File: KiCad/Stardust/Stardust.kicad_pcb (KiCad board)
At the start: 2 copper layers, 7 parts, among them IC1 TS1117BCW50_RPG, U1 ESP32-DEVKITC, U2 TMC2209_SILENTSTEPSTICK, U3 TMC2209_SILENTSTEPSTICK, U4 WEMOS_D1_mini, U5 RTC 3013, U6 MC7812BDTRKG

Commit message: More work on sch and board layout
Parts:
- added J1: Jack-DC, Stardust:DC_PowerConn_694108402002, F.Cu at (189.8, 55.9)
- added J2: 85513-5002, Stardust:RJ12_855135114, F.Cu at (165.0, 58.5)
- added U7: 56200001009, Stardust:FuseHolder_RHDR2W53P0X508_1X2, F.Cu at (183.9, 55.5)
- U1, U2, U3, U4, U5: moved to B.Cu
- moved U4 69.7 mm to (148.4, 59.6), turned to 180 degrees
- moved U2 58.1 mm to (190.5, 115.0)
- moved U5 47.5 mm to (133.3, 114.1), turned to -90 degrees
- moved U1 32.7 mm to (164.3, 100.3), turned to 180 degrees
- moved U3 31.5 mm to (190.7, 93.2)
- moved IC1 25.1 mm to (194.3, 76.0)
- moved U6 14.5 mm to (195.1, 68.5), turned to -90 degrees
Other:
- board outline added: 77 x 77 mm

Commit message: Finished schematic (V1.0)
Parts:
- removed IC1: TS1117BCW50_RPG, Stardust:5VREG_SOT230P700X180-4N
- removed U5: RTC 3013, Stardust:MODULE_3013
- removed U6: MC7812BDTRKG, Stardust:12VREG_DPAK-3_ONS
- added J3: 1x2 Connector, Connector_PinHeader_2.54mm:PinHeader_1x02_P2.54mm_Vertical, F.Cu at (181.0, 73.0)
- added J7: 1x2 Connector, Connector_PinHeader_2.54mm:PinHeader_1x02_P2.54mm_Vertical, F.Cu at (111.6, 53.4)
- added R1: 4.7K, Resistor_SMD:R_0402_1005Metric, F.Cu at (188.0, 79.5)
- added R10: 4.7K, Resistor_SMD:R_0402_1005Metric, F.Cu at (104.9, 58.0)
- added R11: 2.4K, Resistor_SMD:R_0402_1005Metric, F.Cu at (104.9, 60.0)
- added R12: 2.4K, Resistor_SMD:R_0402_1005Metric, F.Cu at (107.8, 52.0)
- added R13: 2.4K, Resistor_SMD:R_0402_1005Metric, F.Cu at (107.8, 54.0)
- added R14: 2.4K, Resistor_SMD:R_0402_1005Metric, F.Cu at (107.8, 56.0)
- added R15: 2.4K, Resistor_SMD:R_0402_1005Metric, F.Cu at (107.8, 58.0)
- added R2: 1K, Resistor_SMD:R_0402_1005Metric, F.Cu at (102.0, 52.0)
- added R3: 4.7K, Resistor_SMD:R_0402_1005Metric, F.Cu at (102.0, 54.0)
- added R4: 4.7K, Resistor_SMD:R_0402_1005Metric, F.Cu at (102.0, 56.0)
- added R5: 4.7K, Resistor_SMD:R_0402_1005Metric, F.Cu at (102.0, 58.0)
- added R6: 4.7K, Resistor_SMD:R_0402_1005Metric, F.Cu at (102.0, 60.0)
- added R7: 4.7K, Resistor_SMD:R_0402_1005Metric, F.Cu at (104.9, 52.0)
- added R8: 4.7K, Resistor_SMD:R_0402_1005Metric, F.Cu at (104.9, 54.0)
- added R9: 4.7K, Resistor_SMD:R_0402_1005Metric, F.Cu at (104.9, 56.0)
- added U8: LittlFuse 2.5 Amp, Stardust:FuseHolder_RHDR2W53P0X508_1X2, F.Cu at (184.5, 68.5)
- J1: value Jack-DC -> 12V DC
- J2: value 85513-5002 -> RJ12
- U1: value ESP32-DEVKITC -> ESP32
- U2, U3: value TMC2209_SILENTSTEPSTICK -> BTT TMC2209 V1.3
- U7: value 56200001009 -> Regulator - 5V 1A; footprint Stardust:FuseHolder_RHDR2W53P0X508_1X2 -> Stardust:5VREG_SOT230P700X180-4N
- moved U7 4.18 mm to (181.5, 58.9)
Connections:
- J1 pad 1: unconnected-(J1-Pad1) -> Net-(J1-Pad1)
- J1 pad 2: unconnected-(J1-Pad2) -> GND
- J1 pad 3: (no net) -> unconnected-(J1-switch-Pad3)
- J2 pad 1: unconnected-(J2-Pad1) -> /RA+
- J2 pad 2: unconnected-(J2-Pad2) -> /DE+
- J2 pad 3: unconnected-(J2-Pad3) -> /DE-
- J2 pad 4: unconnected-(J2-Pad4) -> /RA-
- J2 pad 5: unconnected-(J2-Pad5) -> GND
- J2 pad 6: unconnected-(J2-Pad6) -> Net-(J7-Pin_2)
- U1 pad 1: unconnected-(U1-3V3-Pad1) -> +3.3V
- U1 pad 10: unconnected-(U1-IO26-Pad10) -> /DIR2
- U1 pad 11: unconnected-(U1-IO27-Pad11) -> /STEP2
- U1 pad 12: unconnected-(U1-IO14-Pad12) -> /AUX3
- U1 pad 13: unconnected-(U1-IO12-Pad13) -> /STA
- U1 pad 14: unconnected-(U1-GND1-Pad14) -> GND
- U1 pad 15: unconnected-(U1-IO13-Pad15) -> /AUX4
- U1 pad 19: unconnected-(U1-EXT_5V-Pad19) -> +5V
- U1 pad 2: unconnected-(U1-EN-Pad2) -> /ESP32_RST
- U1 pad 25: unconnected-(U1-IO0-Pad25) -> /DIR1
- U1 pad 26: unconnected-(U1-IO4-Pad26) -> /UART_TX
- U1 pad 27: unconnected-(U1-IO16-Pad27) -> /RX2
- U1 pad 28: unconnected-(U1-IO17-Pad28) -> /TX2
- U1 pad 29: unconnected-(U1-IO5-Pad29) -> /EN
- U1 pad 3: unconnected-(U1-SENSOR_VP-Pad3) -> /PEC
- U1 pad 30: unconnected-(U1-IO18-Pad30) -> /STEP1
- U1 pad 32: unconnected-(U1-GND2-Pad32) -> GND
- U1 pad 33: unconnected-(U1-IO21-Pad33) -> /SDA
- U1 pad 34: unconnected-(U1-RXD0-Pad34) -> /TX0
- U1 pad 35: unconnected-(U1-TXD0-Pad35) -> /RX0
- U1 pad 36: unconnected-(U1-IO22-Pad36) -> /SCL
- U1 pad 37: unconnected-(U1-IO23-Pad37) -> /AUX7
- U1 pad 38: unconnected-(U1-GND3-Pad38) -> GND
- U1 pad 4: unconnected-(U1-SENSOR_VN-Pad4) -> /UART_RX
- U1 pad 5: unconnected-(U1-IO34-Pad5) -> /RA-
- U1 pad 6: unconnected-(U1-IO35-Pad6) -> /RA+
- U1 pad 7: unconnected-(U1-IO32-Pad7) -> /DE-
- U1 pad 8: unconnected-(U1-IO33-Pad8) -> /DE+
- U1 pad 9: unconnected-(U1-IO25-Pad9) -> /AUX8
- U2 pad 1: Net-(U2-GND-Pad1) -> /EN
- U2 pad 10: unconnected-(U2-STEP-Pad10) -> +3.3V
- U2 pad 11: unconnected-(U2-PDN-Pad11) -> /B2_1
- U2 pad 12: unconnected-(U2-UART-Pad12) -> /B1_1
- U2 pad 13: unconnected-(U2-SPRD-Pad13) -> /A1_1
- U2 pad 14: unconnected-(U2-MS2-Pad14) -> /A2_1
- U2 pad 15: unconnected-(U2-MS1-Pad15) -> GND
- U2 pad 16: unconnected-(U2-~{EN}-Pad16) -> +12V
- U2 pad 2: unconnected-(U2-VIO-Pad2) -> GND
- U2 pad 3: unconnected-(U2-M1B-Pad3) -> GND
- U2 pad 4: unconnected-(U2-M1A-Pad4) -> /UART_RX
- U2 pad 7: Net-(U2-GND-Pad1) -> /STEP_1
- U2 pad 8: unconnected-(U2-VM-Pad8) -> /DIR_1
- U2 pad 9: unconnected-(U2-DIR-Pad9) -> GND
- U3 pad 1: Net-(U3-GND-Pad1) -> /EN
- U3 pad 10: unconnected-(U3-STEP-Pad10) -> +3.3V
- U3 pad 11: unconnected-(U3-PDN-Pad11) -> /B2_2
- U3 pad 12: unconnected-(U3-UART-Pad12) -> /B1_2
- U3 pad 13: unconnected-(U3-SPRD-Pad13) -> /A1_2
- U3 pad 14: unconnected-(U3-MS2-Pad14) -> /A2_2
- U3 pad 15: unconnected-(U3-MS1-Pad15) -> GND
- U3 pad 16: unconnected-(U3-~{EN}-Pad16) -> +12V
- U3 pad 2: unconnected-(U3-VIO-Pad2) -> GND
- U3 pad 3: unconnected-(U3-M1B-Pad3) -> +3.3V
- U3 pad 4: unconnected-(U3-M1A-Pad4) -> /UART_RX
- U3 pad 7: Net-(U3-GND-Pad1) -> /STEP_2
- U3 pad 8: unconnected-(U3-VM-Pad8) -> /DIR_2
- U3 pad 9: unconnected-(U3-DIR-Pad9) -> GND
- U4 pad 10: unconnected-(U4-GND-Pad10) -> GND
- U4 pad 13: unconnected-(U4-SDA/D2-Pad13) -> /EN2_B
- U4 pad 14: unconnected-(U4-SCL/D1-Pad14) -> /EN2_A
- U4 pad 4: unconnected-(U4-SCK/D5-Pad4) -> /EN1_A
- U4 pad 5: unconnected-(U4-MISO/D6-Pad5) -> /EN1_B
- U4 pad 6: unconnected-(U4-MOSI/D7-Pad6) -> /TX2
- U4 pad 7: unconnected-(U4-CS/D8-Pad7) -> /RX2
- U4 pad 9: unconnected-(U4-5V-Pad9) -> +5V
- U7 pad 1: unconnected-(U7-Pad1) -> GND

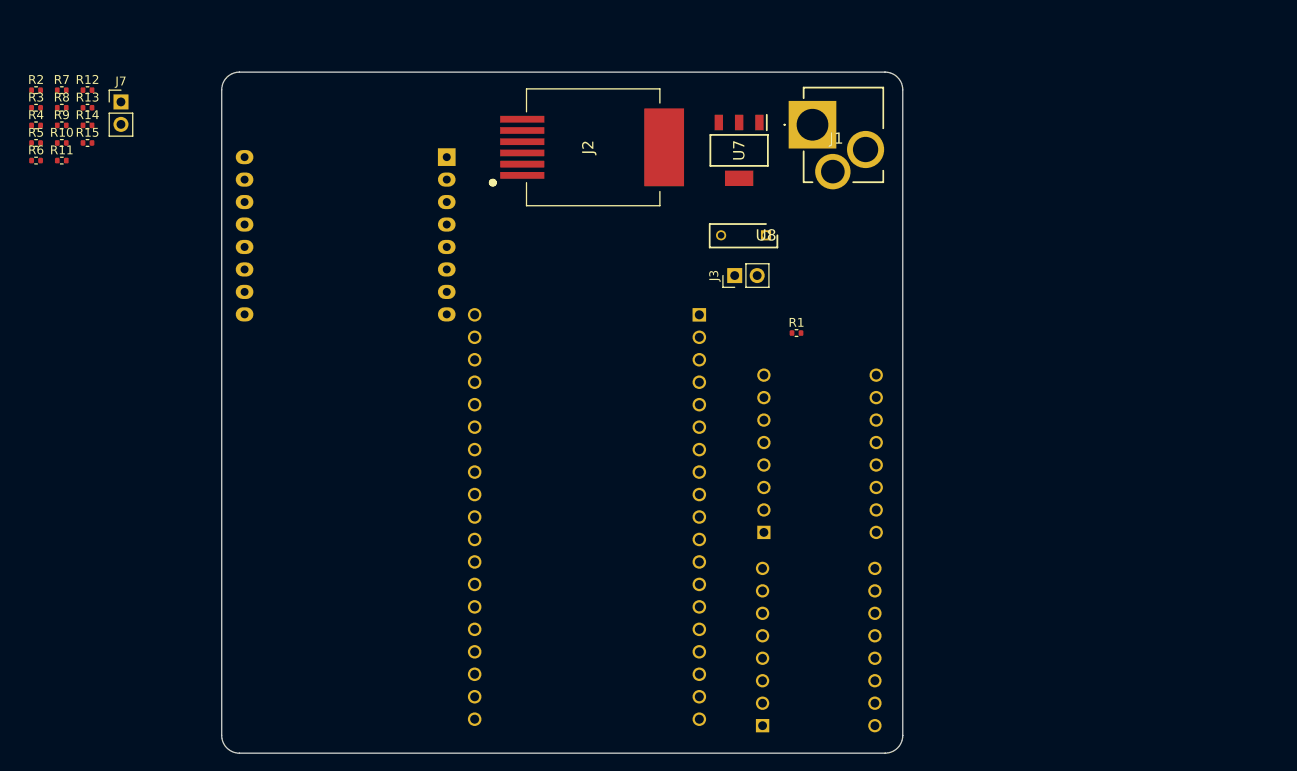
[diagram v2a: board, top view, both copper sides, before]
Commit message: Added parts for everything as well as assigned footprints. Board should be ready to finish
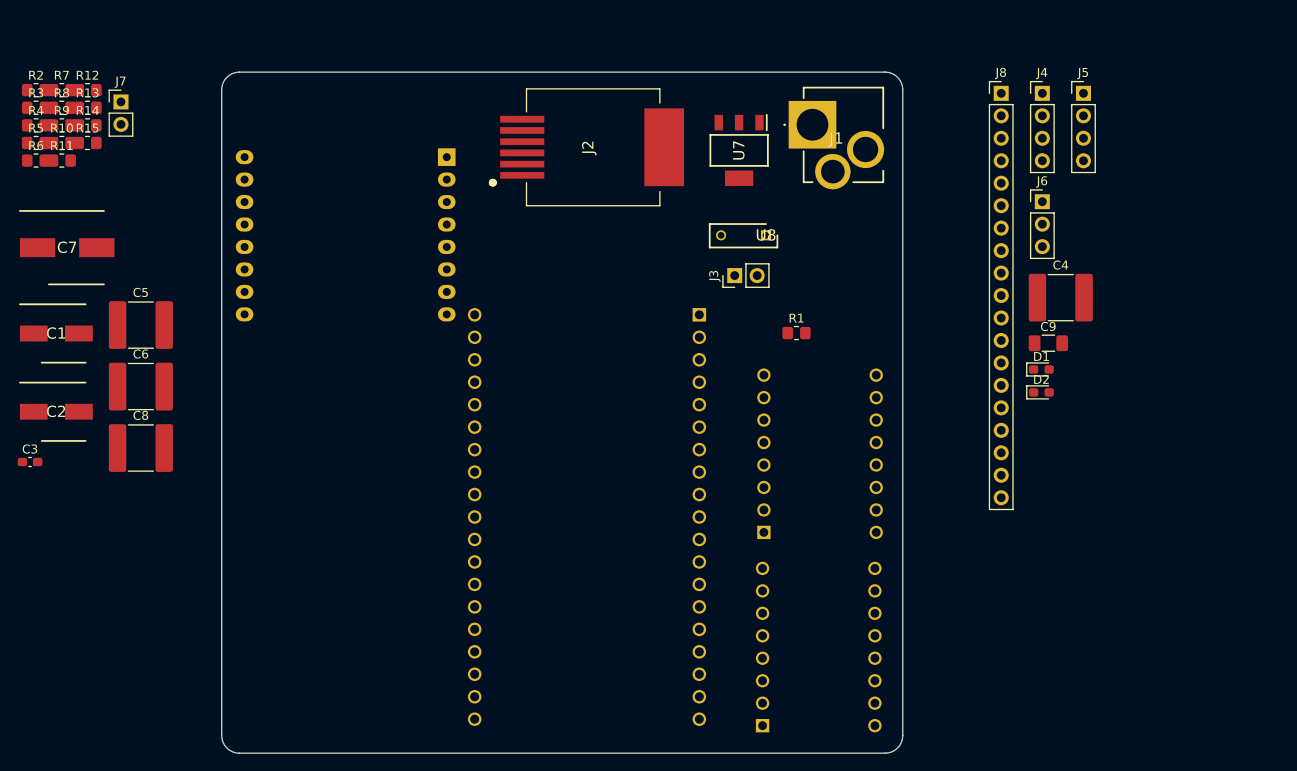
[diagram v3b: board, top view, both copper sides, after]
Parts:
- added C1: 10 uF, Stardust:10uFElectrolyticCap_CAPAE660X550N, F.Cu at (104.3, 79.5)
- added C2: 10 uF, Stardust:10uFElectrolyticCap_CAPAE660X550N, F.Cu at (104.3, 88.4)
- added C3: 10uF, Capacitor_SMD:C_0603_1608Metric_Pad1.08x0.95mm_HandSolder, F.Cu at (101.3, 94.1)
- added C4: 100nF, Capacitor_SMD:C_2220_5750Metric_Pad1.97x5.40mm_HandSolder, F.Cu at (217.9, 75.5)
- added C5: 100nF, Capacitor_SMD:C_2220_5750Metric_Pad1.97x5.40mm_HandSolder, F.Cu at (113.9, 78.6)
- added C6: 100nF, Capacitor_SMD:C_2220_5750Metric_Pad1.97x5.40mm_HandSolder, F.Cu at (113.9, 85.5)
- added C7: 100 uF, Stardust:100uFElectrolyticCap_CAPAE830X1080N, F.Cu at (105.5, 69.8)
- added C8: 100nF, Capacitor_SMD:C_2220_5750Metric_Pad1.97x5.40mm_HandSolder, F.Cu at (113.9, 92.5)
- added C9: 330nF, Capacitor_SMD:C_1206_3216Metric_Pad1.33x1.80mm_HandSolder, F.Cu at (216.5, 80.7)
- added D1: PWR LED, LED_SMD:LED_0603_1608Metric_Pad1.05x0.95mm_HandSolder, F.Cu at (215.7, 83.6)
- added D2: STATUS LED, LED_SMD:LED_0603_1608Metric_Pad1.05x0.95mm_HandSolder, F.Cu at (215.7, 86.2)
- added J4: Conn_01x04_Pin, Connector_PinHeader_2.54mm:PinHeader_1x04_P2.54mm_Vertical, F.Cu at (215.8, 52.4)
- added J5: Conn_01x04_Pin, Connector_PinHeader_2.54mm:PinHeader_1x04_P2.54mm_Vertical, F.Cu at (220.4, 52.4)
- added J6: 1x3 Header, Connector_PinHeader_2.54mm:PinHeader_1x03_P2.54mm_Vertical, F.Cu at (215.8, 64.7)
- added J8: Conn_01x19_Pin, Connector_PinHeader_2.54mm:PinHeader_1x19_P2.54mm_Vertical, F.Cu at (211.1, 52.4)
- R1, R10, R11, R12, R13, R14, R15, R2, R3, R4, R5, R6, R7, R8, R9: footprint Resistor_SMD:R_0402_1005Metric -> Resistor_SMD:R_0805_2012Metric_Pad1.20x1.40mm_HandSolder

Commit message: Finished board design and created gerber files
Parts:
- removed R8: 4.7K, Resistor_SMD:R_0805_2012Metric_Pad1.20x1.40mm_HandSolder
- J4, J5, J6, J8, R4, R5, R6, R7: moved to B.Cu
- moved R9 108.4 mm to (190.0, 123.2), turned to -90 degrees
- moved R10 104.8 mm to (187.0, 123.2), turned to -90 degrees
- moved J5 97.0 mm to (151.0, 120.1)
- moved R15 87.4 mm to (186.0, 97.0)
- moved C3 85.6 mm to (185.6, 79.5), turned to 180 degrees
- moved J4 82.4 mm to (151.0, 103.3)
- moved R2 80.6 mm to (160.5, 107.5)
- moved R3 77.6 mm to (160.5, 105.0)
- moved C7 76.1 mm to (180.5, 56.9), turned to -90 degrees
- moved C6 69.4 mm to (176.2, 116.0), turned to 90 degrees
- moved C8 68.4 mm to (171.8, 56.0), turned to -90 degrees
- moved C2 67.5 mm to (163.5, 56.0), turned to -90 degrees
- moved C5 67.0 mm to (176.8, 101.8), turned to -90 degrees
- moved J6 62.8 mm to (153.0, 67.5), turned to 180 degrees
- moved U3 59.5 mm to (135.9, 116.3), turned to 90 degrees
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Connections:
- J6 pad 1: unconnected-(J6-Pin_1-Pad1) -> GND
- J6 pad 2: unconnected-(J6-Pin_2-Pad2) -> /PUL
- J6 pad 3: unconnected-(J6-Pin_3-Pad3) -> +3.3V
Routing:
- net +3.3V: track 0.00 -> 238.1 mm
- net +5V: track 0.00 -> 190.1 mm
- net GND: track 0.00 -> 117.2 mm, vias 0 -> 11
- net /EN2_A: track 0.00 -> 101.6 mm, vias 0 -> 2
- net /UART_RX: track 0.00 -> 95.2 mm
- net /EN2_B: track 0.00 -> 90.7 mm
- net /AUX7: track 0.00 -> 73.7 mm, vias 0 -> 4
- net /EN1_B: track 0.00 -> 66.1 mm, vias 0 -> 2
- net /EN1_A: track 0.00 -> 62.9 mm
- net /RA-: track 0.00 -> 60.9 mm, vias 0 -> 1
- net /DE+: track 0.00 -> 59.1 mm, vias 0 -> 3
- net /DE-: track 0.00 -> 58.2 mm, vias 0 -> 1
- net /SCL: track 0.00 -> 51.2 mm, vias 0 -> 2
- net /RA+: track 0.00 -> 49.1 mm, vias 0 -> 1
- net /RX0: track 0.00 -> 48.9 mm, vias 0 -> 4
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- added copper zone on F.Cu, net +12V
- added copper zone on B.Cu, net GND
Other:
- board text added: "15V MAX"
- board text added: "5V PWR"
- board text added: "AX1 RA"
- board text added: "AX2 DEC"
- board text added: "ESP32"
- board text added: "PWR"
- board text added: "STATUS"
- board text added: "TMC2209"
- board text added: "UP DWN"

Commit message: Added silkscreen images
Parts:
- added G1: LOGO, images:logo_footprint, F.Cu at (169.8, 86.9)
- added G1: LOGO, images:logo_footprint, B.Cu at (168.9, 60.8)
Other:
- board text added: "Isaac Bosley 2025"

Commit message: Added bom and replaced expensive cap
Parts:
- C4, C5, C6, C8: footprint Capacitor_SMD:C_2220_5750Metric_Pad1.97x5.40mm_HandSolder -> Capacitor_SMD:C_0805_2012Metric_Pad1.18x1.45mm_HandSolder
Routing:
- net GND: track 117.2 -> 123.5 mm
- net /AUX3: track 34.4 -> 35.2 mm
- net /PEC: track 37.4 -> 38.0 mm
- net /AUX4: track 37.6 -> 38.2 mm

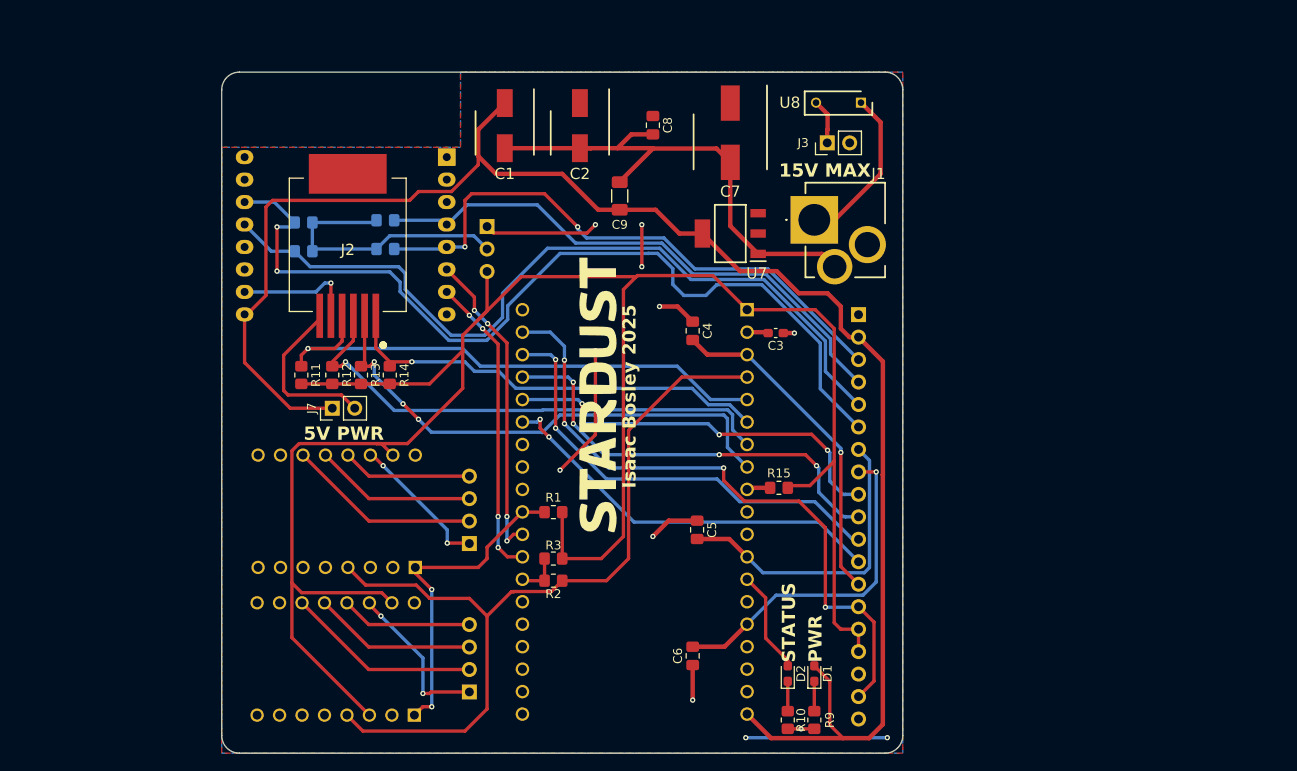
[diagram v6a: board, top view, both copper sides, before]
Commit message: Fixed some power plane issues and added mounting holes
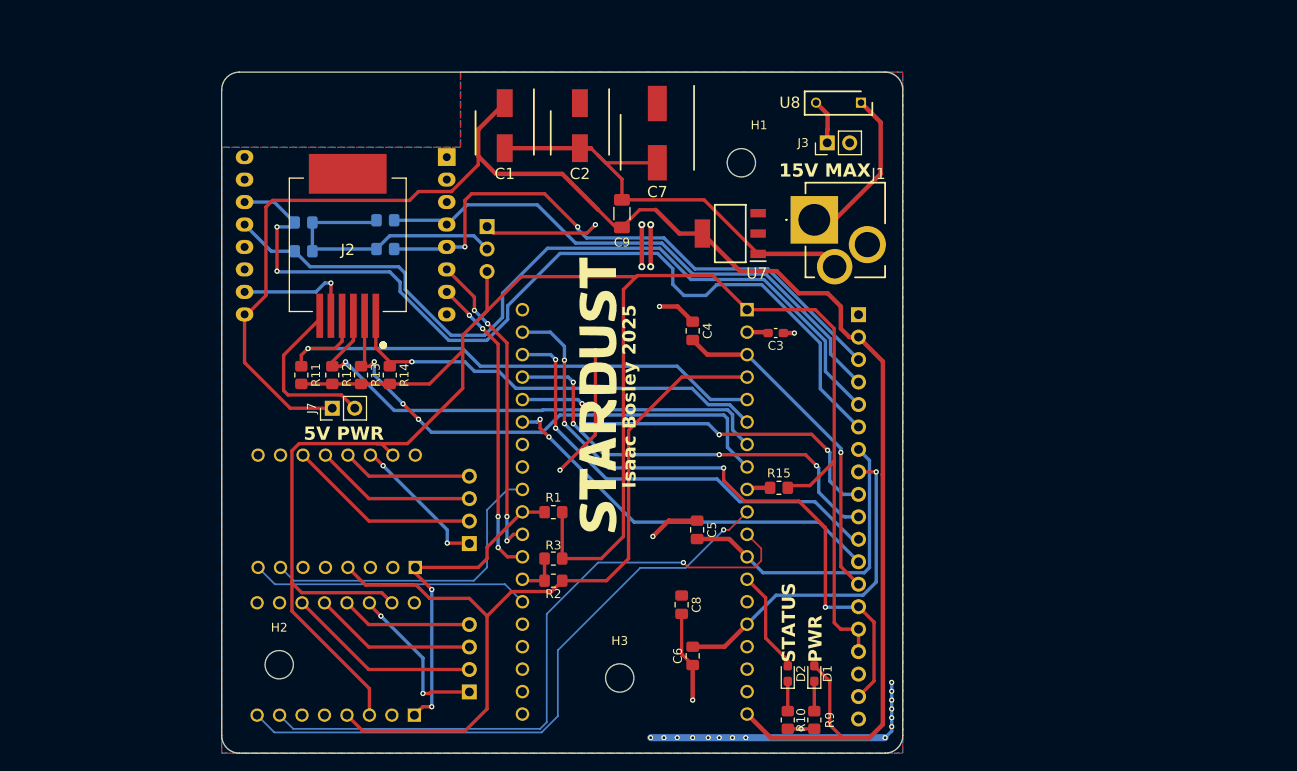
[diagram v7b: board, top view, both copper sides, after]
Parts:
- added H1: MountingHole, MountingHole:MountingHole_3.2mm_M3, F.Cu at (181.8, 60.2)
- added H2: MountingHole, MountingHole:MountingHole_3.2mm_M3, F.Cu at (129.5, 117.0)
- added H3: MountingHole, MountingHole:MountingHole_3.2mm_M3, F.Cu at (168.0, 118.5)
- moved C8 54.3 mm to (175.0, 110.2)
- moved C7 8.25 mm to (172.2, 56.9)
- moved G1 3.72 mm to (166.1, 58.3)
- moved C9 2.02 mm to (168.2, 66.0)
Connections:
- U2 pad 7: /STEP_1 -> /STEP1
- U2 pad 8: /DIR_1 -> /DIR1
- U3 pad 7: /STEP_2 -> /STEP2
- U3 pad 8: /DIR_2 -> /DIR2
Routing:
- net /STEP2: track 0.00 -> 74.3 mm, vias 0 -> 1
- net /DIR2: track 0.00 -> 70.9 mm, vias 0 -> 1
- net /STEP1: track 0.00 -> 36.1 mm
- net /DIR1: track 0.00 -> 31.5 mm
- net +12V: track 16.2 -> 33.1 mm, vias 2 -> 15
- net GND: track 123.5 -> 128.7 mm, vias 11 -> 13
- net +5V: track 190.1 -> 191.7 mm
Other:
- board text added: "+3.3V"
- board text added: "5V"
- board text added: "AUX3"
- board text added: "AUX4"
- board text added: "AUX7"
- board text added: "EN1_A"
- board text added: "EN1_B"
- board text added: "EN2_A"
- board text added: "EN2_B"
- board text added: "LIMIT"
- board text added: "PEC"
- board text added: "PPS"
- board text added: "RX0"
- board text added: "SCL"
- board text added: "SDA"
- board text added: "TX0"
